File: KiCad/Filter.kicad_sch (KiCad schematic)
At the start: 25 parts, among them U5 TL074, U6 TL074

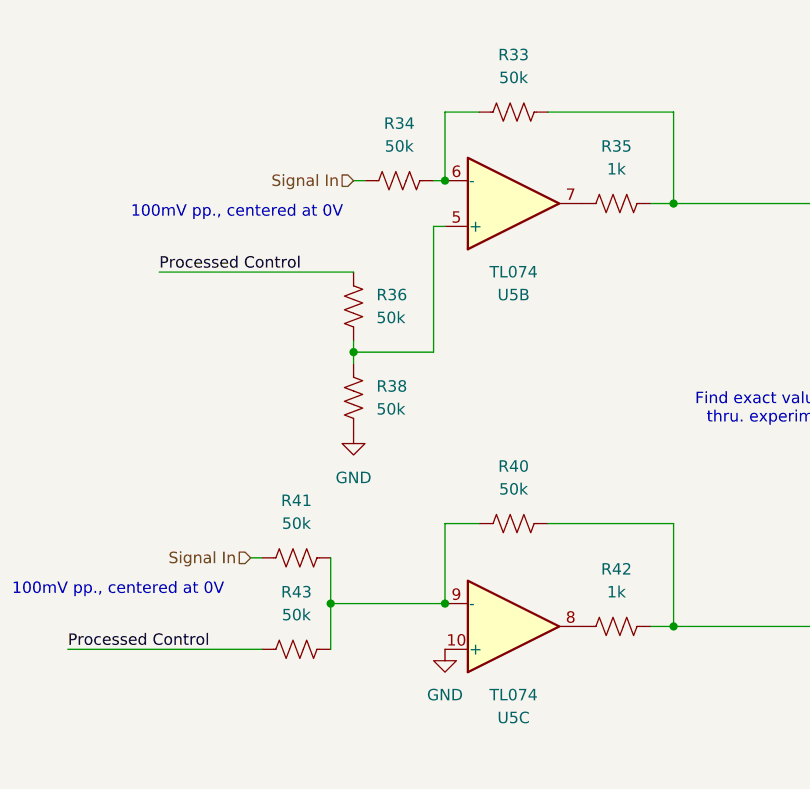
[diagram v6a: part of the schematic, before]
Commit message: updated footprints
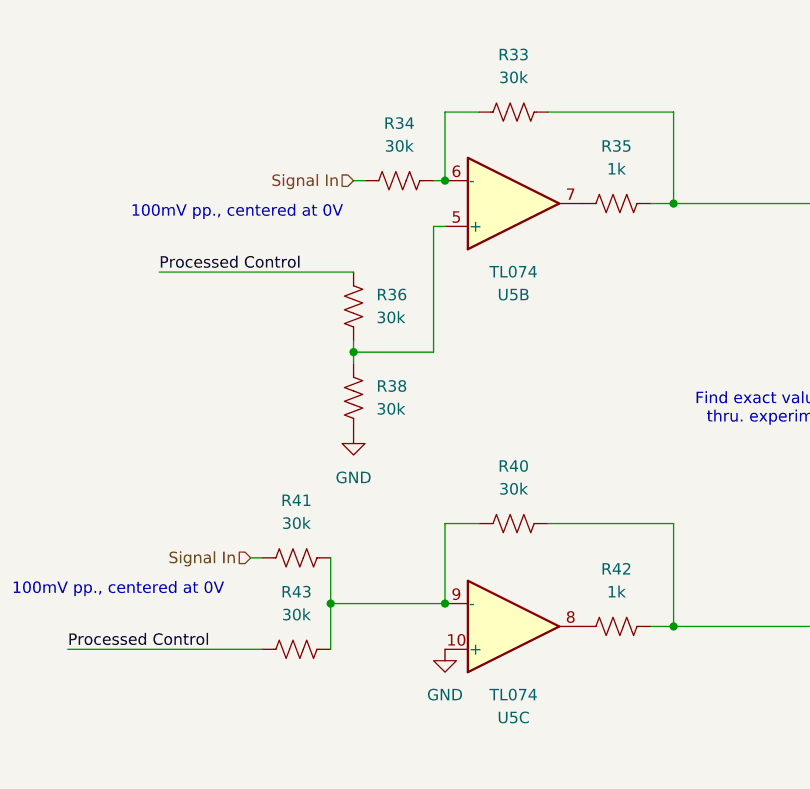
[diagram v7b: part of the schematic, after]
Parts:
- C5, C6, C7: footprint (none) -> Capacitor_THT:C_Rect_L18.0mm_W5.0mm_P15.00mm_FKS3_FKP3
- R33, R34, R36, R38, R40, R41, R43: value 50k -> 30k; footprint (none) -> Resistor_SMD:R_0201_0603Metric
- R35, R42: footprint (none) -> Resistor_SMD:R_0402_1005Metric
- R37, R39, R44, R45: footprint (none) -> Resistor_THT:R_Axial_DIN0207_L6.3mm_D2.5mm_P7.62mm_Horizontal
- U5, U6: footprint (none) -> Package_DIP:DIP-14_W7.62mm
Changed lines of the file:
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@@
 		(dnp no)
 		(fields_autoplaced yes)
-		(property "Reference" "#PWR037"
+		(property "Reference" "#PWR036"
 			(at 234.95 96.52 0)
 			(hide yes)
@@
 			(project "Electronic Trombone"
 				(path "/931827f3-33b7-460f-8885-7db258da2648/6d65ef8f-8235-46d4-95e7-69caf9b93e91"
-					(reference "#PWR037")
+					(reference "#PWR036")
 					(unit 1)
 				)
@@
 			)
 		)
-		(property "Footprint" ""
+		(property "Footprint" "Package_DIP:DIP-14_W7.62mm"
 			(at 91.44 74.93 0)
 			(hide yes)
@@
 			)
 		)
-		(property "Footprint" ""
+		(property "Footprint" "Resistor_THT:R_Axial_DIN0207_L6.3mm_D2.5mm_P7.62mm_Horizontal"
 			(at 61.214 151.384 90)
 			(hide yes)
@@
 			)
 		)
-		(property "Footprint" ""
+		(property "Footprint" "Resistor_THT:R_Axial_DIN0207_L6.3mm_D2.5mm_P7.62mm_Horizontal"
 			(at 76.454 142.494 90)
 			(hide yes)
@@
 		(dnp no)
 		(fields_autoplaced yes)
-		(property "Reference" "#PWR035"
+		(property "Reference" "#PWR034"
 			(at 171.45 85.09 0)
 			(hide yes)
@@
 			(project "Electronic Trombone"
 				(path "/931827f3-33b7-460f-8885-7db258da2648/6d65ef8f-8235-46d4-95e7-69caf9b93e91"
-					(reference "#PWR035")
+					(reference "#PWR034")
 					(unit 1)
 				)
@@
 			)
 		)
-		(property "Value" "50k"
+		(property "Value" "30k"
 			(at 189.23 39.37 90)
 			(show_name no)
@@
 			)
 		)
-		(property "Footprint" ""
+		(property "Footprint" "Resistor_SMD:R_0201_0603Metric"
 			(at 189.484 42.164 90)
 			(hide yes)
@@
 			)
 		)
-		(property "Footprint" ""
+		(property "Footprint" "Capacitor_THT:C_Rect_L18.0mm_W5.0mm_P15.00mm_FKS3_FKP3"
 			(at 245.11 76.5048 0)
 			(hide yes)
@@
 			)
 		)
-		(property "Footprint" ""
+		(property "Footprint" "Capacitor_THT:C_Rect_L18.0mm_W5.0mm_P15.00mm_FKS3_FKP3"
 			(at 245.11 63.8048 0)
 			(hide yes)
@@
 		(dnp no)
 		(fields_autoplaced yes)
-		(property "Reference" "#PWR033"
+		(property "Reference" "#PWR032"
 			(at 234.95 71.12 0)
 			(hide yes)
@@
 			(project "Electronic Trombone"
 				(path "/931827f3-33b7-460f-8885-7db258da2648/6d65ef8f-8235-46d4-95e7-69caf9b93e91"
-					(reference "#PWR033")
+					(reference "#PWR032")
 					(unit 1)
 				)
@@
 			)
 		)
-		(property "Value" "50k"
+		(property "Value" "30k"
 			(at 173.99 66.0399 0)
 			(show_name no)
@@
 			)
 		)
-		(property "Footprint" ""
+		(property "Footprint" "Resistor_SMD:R_0201_0603Metric"
 			(at 170.434 64.516 90)
 			(hide yes)
@@
 			)
 		)
-		(property "Footprint" ""
+		(property "Footprint" "Capacitor_THT:C_Rect_L18.0mm_W5.0mm_P15.00mm_FKS3_FKP3"
 			(at 245.11 89.2048 0)
 			(hide yes)
@@
 			)
 		)
-		(property "Footprint" ""
+		(property "Footprint" "Package_DIP:DIP-14_W7.62mm"
 			(at 74.93 157.48 0)
 			(hide yes)
@@
 			)
 		)
-		(property "Footprint" ""
+		(property "Footprint" "Resistor_THT:R_Axial_DIN0207_L6.3mm_D2.5mm_P7.62mm_Horizontal"
 			(at 53.594 68.326 90)
 			(hide yes)
@@
 			)
 		)
-		(property "Value" "50k"
+		(property "Value" "30k"
 			(at 165.1 88.9 90)
 			(show_name no)
@@
 			)
 		)
-		(property "Footprint" ""
+		(property "Footprint" "Resistor_SMD:R_0201_0603Metric"
 			(at 165.354 91.694 90)
 			(hide yes)
@@
 		(dnp no)
 		(fields_autoplaced yes)
-		(property "Reference" "#PWR038"
+		(property "Reference" "#PWR037"
 			(at 68.58 104.14 0)
 			(hide yes)
@@
 			(project "Electronic Trombone"
 				(path "/931827f3-33b7-460f-8885-7db258da2648/6d65ef8f-8235-46d4-95e7-69caf9b93e91"
-					(reference "#PWR038")
+					(reference "#PWR037")
 					(unit 1)
 				)
@@
 			)
 		)
-		(property "Footprint" ""
+		(property "Footprint" "Resistor_SMD:R_0402_1005Metric"
 			(at 200.406 101.346 90)
 			(hide yes)
@@
 			)
 		)
-		(property "Footprint" ""
+		(property "Footprint" "Package_DIP:DIP-14_W7.62mm"
 			(at 44.45 149.86 0)
 			(hide yes)
@@
 			)
 		)
-		(property "Footprint" ""
+		(property "Footprint" "Package_DIP:DIP-14_W7.62mm"
 			(at 187.96 102.87 0)
 			(hide yes)
@@
 		(dnp no)
 		(fields_autoplaced yes)
-		(property "Reference" "#PWR039"
+		(property "Reference" "#PWR038"
 			(at 181.61 109.22 0)
 			(hide yes)
@@
 			(project "Electronic Trombone"
 				(path "/931827f3-33b7-460f-8885-7db258da2648/6d65ef8f-8235-46d4-95e7-69caf9b93e91"
-					(reference "#PWR039")
+					(reference "#PWR038")
 					(unit 1)
 				)
@@
 			)
 		)
-		(property "Footprint" ""
+		(property "Footprint" "Package_DIP:DIP-14_W7.62mm"
 			(at 95.25 154.94 0)
 			(hide yes)
@@
 		(dnp no)
 		(fields_autoplaced yes)
-		(property "Reference" "#PWR036"
+		(property "Reference" "#PWR035"
 			(at 54.61 91.44 0)
 			(hide yes)
@@
 			(project "Electronic Trombone"
 				(path "/931827f3-33b7-460f-8885-7db258da2648/6d65ef8f-8235-46d4-95e7-69caf9b93e91"
-					(reference "#PWR036")
+					(reference "#PWR035")
 					(unit 1)
 				)
@@
 			)
 		)
-		(property "Value" "50k"
+		(property "Value" "30k"
 			(at 189.23 85.09 90)
 			(show_name no)
@@
 			)
 		)
-		(property "Footprint" ""
+		(property "Footprint" "Resistor_SMD:R_0201_0603Metric"
 			(at 189.484 87.884 90)
 			(hide yes)
@@
 			)
 		)
-		(property "Footprint" ""
+		(property "Footprint" "Package_DIP:DIP-14_W7.62mm"
 			(at 187.96 55.88 0)
 			(hide yes)
@@
 		(dnp no)
 		(fields_autoplaced yes)
-		(property "Reference" "#PWR034"
+		(property "Reference" "#PWR033"
 			(at 234.95 83.82 0)
 			(hide yes)
@@
 			(project "Electronic Trombone"
 				(path "/931827f3-33b7-460f-8885-7db258da2648/6d65ef8f-8235-46d4-95e7-69caf9b93e91"
-					(reference "#PWR034")
+					(reference "#PWR033")
 					(unit 1)
 				)
@@
 		(dnp no)
 		(fields_autoplaced yes)
-		(property "Reference" "#PWR040"
+		(property "Reference" "#PWR039"
 			(at 68.58 163.83 0)
 			(hide yes)
@@
 			(project "Electronic Trombone"
 				(path "/931827f3-33b7-460f-8885-7db258da2648/6d65ef8f-8235-46d4-95e7-69caf9b93e91"
-					(reference "#PWR040")
+					(reference "#PWR039")
 					(unit 1)
 				)
@@
 			)
 		)
-		(property "Footprint" ""
+		(property "Footprint" "Resistor_THT:R_Axial_DIN0207_L6.3mm_D2.5mm_P7.62mm_Horizontal"
 			(at 53.594 81.026 90)
 			(hide yes)
@@
 			)
 		)
-		(property "Value" "50k"
+		(property "Value" "30k"
 			(at 165.1 99.06 90)
 			(show_name no)
@@
 			)
 		)
-		(property "Footprint" ""
+		(property "Footprint" "Resistor_SMD:R_0201_0603Metric"
 			(at 165.354 101.854 90)
 			(hide yes)
@@
 			)
 		)
-		(property "Value" "50k"
+		(property "Value" "30k"
 			(at 173.99 76.1999 0)
 			(show_name no)
@@
 			)
 		)
-		(property "Footprint" ""
+		(property "Footprint" "Resistor_SMD:R_0201_0603Metric"
 			(at 170.434 74.676 90)
 			(hide yes)
@@
 			)
 		)
-		(property "Value" "50k"
+		(property "Value" "30k"
 			(at 176.53 46.99 90)
 			(show_name no)
@@
 			)
 		)
-		(property "Footprint" ""
+		(property "Footprint" "Resistor_SMD:R_0201_0603Metric"
 			(at 176.784 49.784 90)
 			(hide yes)
@@
 			)
 		)
-		(property "Footprint" ""
+		(property "Footprint" "Resistor_SMD:R_0402_1005Metric"
 			(at 200.406 54.356 90)
 			(hide yes)
